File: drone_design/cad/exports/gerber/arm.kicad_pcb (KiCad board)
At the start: 2 copper layers, 245 x 25 mm, 4 parts

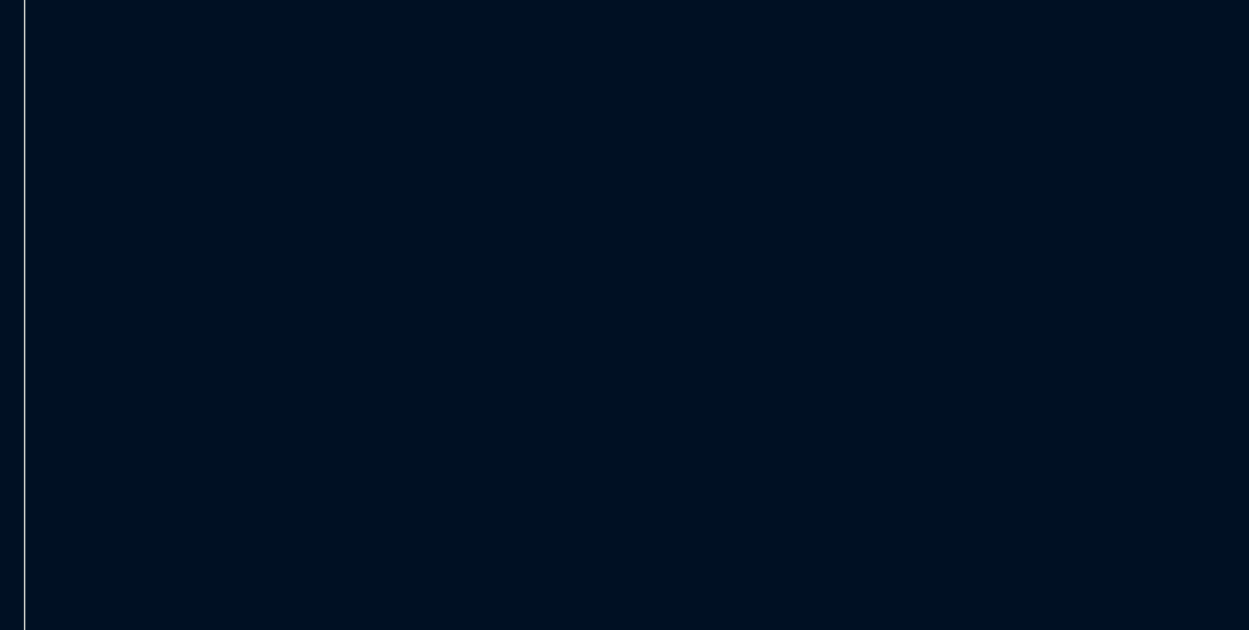
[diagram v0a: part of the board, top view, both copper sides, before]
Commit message: feat: fix ToF bracket alignment, add motor mount to arm tips
- Fix all 6 ToF sensor/bracket positions with correct rotations
  so sensors sit flush against bracket tab faces, sensing outward
- Add circular motor mounting plate at arm tips (25mm dia)
  with 4x M2 bolt holes on 16mm circle + center shaft clearance
- Add matching M2 threaded holes to motor base plate model
- Rebuild all STLs and viewer (68 parts, 15.8 MB total)
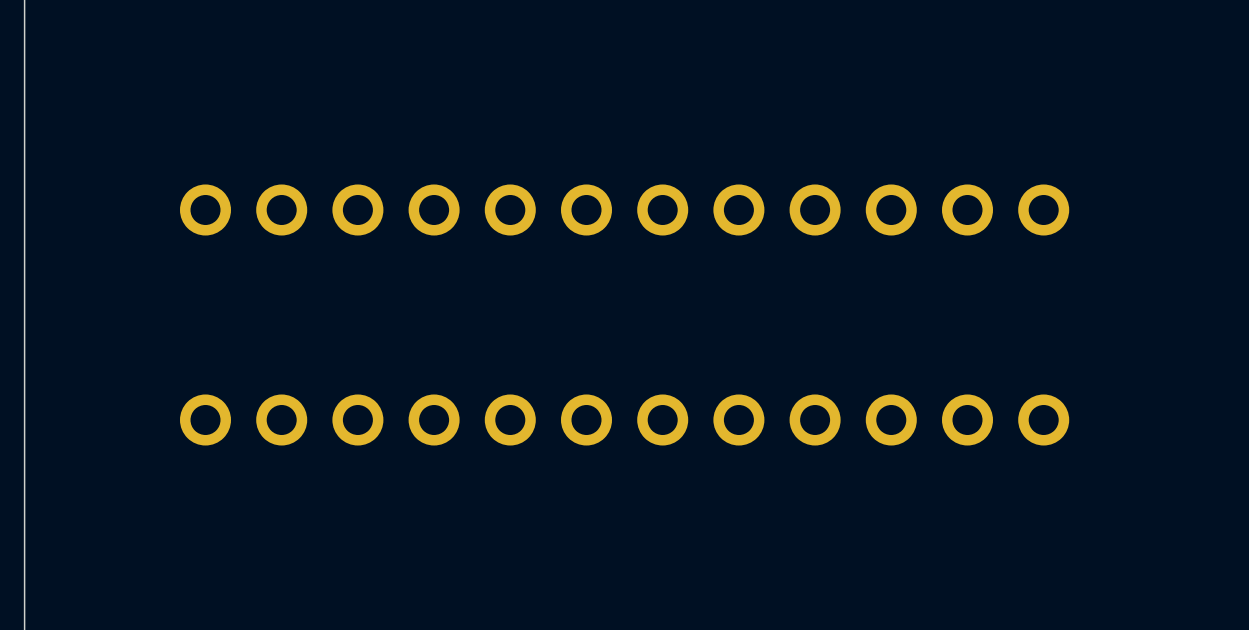
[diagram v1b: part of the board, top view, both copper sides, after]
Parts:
- added ?: , MountingHole:MountingHole_1.0mm, F.Cu at (-103.8, -3.50)
- added ?: , MountingHole:MountingHole_1.0mm, F.Cu at (-101.2, -3.50)
- added ?: , MountingHole:MountingHole_1.0mm, F.Cu at (-98.7, -3.50)
- added ?: , MountingHole:MountingHole_1.0mm, F.Cu at (-96.2, -3.50)
- added ?: , MountingHole:MountingHole_1.0mm, F.Cu at (-93.6, -3.50)
- added ?: , MountingHole:MountingHole_1.0mm, F.Cu at (-91.1, -3.50)
- added ?: , MountingHole:MountingHole_1.0mm, F.Cu at (-88.5, -3.50)
- added ?: , MountingHole:MountingHole_1.0mm, F.Cu at (-116.5, 3.50)
- added ?: , MountingHole:MountingHole_1.0mm, F.Cu at (-113.9, 3.50)
- added ?: , MountingHole:MountingHole_1.0mm, F.Cu at (-111.4, 3.50)
- added ?: , MountingHole:MountingHole_1.0mm, F.Cu at (-108.8, 3.50)
- added ?: , MountingHole:MountingHole_1.0mm, F.Cu at (-106.3, 3.50)
- added ?: , MountingHole:MountingHole_1.0mm, F.Cu at (-103.8, 3.50)
- added ?: , MountingHole:MountingHole_1.0mm, F.Cu at (-101.2, 3.50)
- added ?: , MountingHole:MountingHole_1.0mm, F.Cu at (-98.7, 3.50)
- added ?: , MountingHole:MountingHole_1.0mm, F.Cu at (-96.2, 3.50)
- added ?: , MountingHole:MountingHole_1.0mm, F.Cu at (-93.6, 3.50)
- added ?: , MountingHole:MountingHole_1.0mm, F.Cu at (-91.1, 3.50)
- added ?: , MountingHole:MountingHole_1.0mm, F.Cu at (-88.5, 3.50)
- added ?: , MountingHole:MountingHole_1.0mm, F.Cu at (-116.5, -3.50)
- added ?: , MountingHole:MountingHole_1.0mm, F.Cu at (-113.9, -3.50)
- added ?: , MountingHole:MountingHole_1.0mm, F.Cu at (-111.4, -3.50)
- added ?: , MountingHole:MountingHole_1.0mm, F.Cu at (-108.8, -3.50)
- added ?: , MountingHole:MountingHole_1.0mm, F.Cu at (-106.3, -3.50)
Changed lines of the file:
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@@
+    )
+  )
+  (footprint "MountingHole:MountingHole_1.0mm" (layer "F.Cu")
+    (at -116.4700 -3.5000)
+    (pad "" thru_hole circle (at 0 0) (size 1.70 1.70) (drill 1.00)
+      (layers "*.Cu" "*.Mask")
+    )
+  )
+  (footprint "MountingHole:MountingHole_1.0mm" (layer "F.Cu")
+    (at -113.9300 -3.5000)
+    (pad "" thru_hole circle (at 0 0) (size 1.70 1.70) (drill 1.00)
+      (layers "*.Cu" "*.Mask")
+    )
+  )
+  (footprint "MountingHole:MountingHole_1.0mm" (layer "F.Cu")
+    (at -111.3900 -3.5000)
+    (pad "" thru_hole circle (at 0 0) (size 1.70 1.70) (drill 1.00)
+      (layers "*.Cu" "*.Mask")
+    )
+  )
+  (footprint "MountingHole:MountingHole_1.0mm" (layer "F.Cu")
+    (at -108.8500 -3.5000)
+    (pad "" thru_hole circle (at 0 0) (size 1.70 1.70) (drill 1.00)
+      (layers "*.Cu" "*.Mask")
+    )
+  )
+  (footprint "MountingHole:MountingHole_1.0mm" (layer "F.Cu")
+    (at -106.3100 -3.5000)
+    (pad "" thru_hole circle (at 0 0) (size 1.70 1.70) (drill 1.00)
+      (layers "*.Cu" "*.Mask")
+    )
+  )
+  (footprint "MountingHole:MountingHole_1.0mm" (layer "F.Cu")
+    (at -103.7700 -3.5000)
+    (pad "" thru_hole circle (at 0 0) (size 1.70 1.70) (drill 1.00)
+      (layers "*.Cu" "*.Mask")
+    )
+  )
+  (footprint "MountingHole:MountingHole_1.0mm" (layer "F.Cu")
+    (at -101.2300 -3.5000)
+    (pad "" thru_hole circle (at 0 0) (size 1.70 1.70) (drill 1.00)
+      (layers "*.Cu" "*.Mask")
+    )
+  )
+  (footprint "MountingHole:MountingHole_1.0mm" (layer "F.Cu")
+    (at -98.6900 -3.5000)
+    (pad "" thru_hole circle (at 0 0) (size 1.70 1.70) (drill 1.00)
+      (layers "*.Cu" "*.Mask")
+    )
+  )
+  (footprint "MountingHole:MountingHole_1.0mm" (layer "F.Cu")
+    (at -96.1500 -3.5000)
+    (pad "" thru_hole circle (at 0 0) (size 1.70 1.70) (drill 1.00)
+      (layers "*.Cu" "*.Mask")
+    )
+  )
+  (footprint "MountingHole:MountingHole_1.0mm" (layer "F.Cu")
+    (at -93.6100 -3.5000)
+    (pad "" thru_hole circle (at 0 0) (size 1.70 1.70) (drill 1.00)
+      (layers "*.Cu" "*.Mask")
+    )
+  )
+  (footprint "MountingHole:MountingHole_1.0mm" (layer "F.Cu")
+    (at -91.0700 -3.5000)
+    (pad "" thru_hole circle (at 0 0) (size 1.70 1.70) (drill 1.00)
+      (layers "*.Cu" "*.Mask")
+    )
+  )
+  (footprint "MountingHole:MountingHole_1.0mm" (layer "F.Cu")
+    (at -88.5300 -3.5000)
+    (pad "" thru_hole circle (at 0 0) (size 1.70 1.70) (drill 1.00)
+      (layers "*.Cu" "*.Mask")
+    )
+  )
+  (footprint "MountingHole:MountingHole_1.0mm" (layer "F.Cu")
+    (at -116.4700 3.5000)
+    (pad "" thru_hole circle (at 0 0) (size 1.70 1.70) (drill 1.00)
+      (layers "*.Cu" "*.Mask")
+    )
+  )
+  (footprint "MountingHole:MountingHole_1.0mm" (layer "F.Cu")
+    (at -113.9300 3.5000)
+    (pad "" thru_hole circle (at 0 0) (size 1.70 1.70) (drill 1.00)
+      (layers "*.Cu" "*.Mask")
+    )
+  )
+  (footprint "MountingHole:MountingHole_1.0mm" (layer "F.Cu")
+    (at -111.3900 3.5000)
+    (pad "" thru_hole circle (at 0 0) (size 1.70 1.70) (drill 1.00)
+      (layers "*.Cu" "*.Mask")
+    )
+  )
+  (footprint "MountingHole:MountingHole_1.0mm" (layer "F.Cu")
+    (at -108.8500 3.5000)
+    (pad "" thru_hole circle (at 0 0) (size 1.70 1.70) (drill 1.00)
+      (layers "*.Cu" "*.Mask")
+    )
+  )
+  (footprint "MountingHole:MountingHole_1.0mm" (layer "F.Cu")
+    (at -106.3100 3.5000)
+    (pad "" thru_hole circle (at 0 0) (size 1.70 1.70) (drill 1.00)
+      (layers "*.Cu" "*.Mask")
+    )
+  )
+  (footprint "MountingHole:MountingHole_1.0mm" (layer "F.Cu")
+    (at -103.7700 3.5000)
+    (pad "" thru_hole circle (at 0 0) (size 1.70 1.70) (drill 1.00)
+      (layers "*.Cu" "*.Mask")
+    )
+  )
+  (footprint "MountingHole:MountingHole_1.0mm" (layer "F.Cu")
+    (at -101.2300 3.5000)
+    (pad "" thru_hole circle (at 0 0) (size 1.70 1.70) (drill 1.00)
+      (layers "*.Cu" "*.Mask")
+    )
+  )
+  (footprint "MountingHole:MountingHole_1.0mm" (layer "F.Cu")
+    (at -98.6900 3.5000)
+    (pad "" thru_hole circle (at 0 0) (size 1.70 1.70) (drill 1.00)
+      (layers "*.Cu" "*.Mask")
+    )
+  )
+  (footprint "MountingHole:MountingHole_1.0mm" (layer "F.Cu")
+    (at -96.1500 3.5000)
+    (pad "" thru_hole circle (at 0 0) (size 1.70 1.70) (drill 1.00)
+      (layers "*.Cu" "*.Mask")
+    )
+  )
+  (footprint "MountingHole:MountingHole_1.0mm" (layer "F.Cu")
+    (at -93.6100 3.5000)
+    (pad "" thru_hole circle (at 0 0) (size 1.70 1.70) (drill 1.00)
+      (layers "*.Cu" "*.Mask")
+    )
+  )
+  (footprint "MountingHole:MountingHole_1.0mm" (layer "F.Cu")
+    (at -91.0700 3.5000)
+    (pad "" thru_hole circle (at 0 0) (size 1.70 1.70) (drill 1.00)
+      (layers "*.Cu" "*.Mask")
+    )
+  )
+  (footprint "MountingHole:MountingHole_1.0mm" (layer "F.Cu")
+    (at -88.5300 3.5000)
+    (pad "" thru_hole circle (at 0 0) (size 1.70 1.70) (drill 1.00)
+      (layers "*.Cu" "*.Mask")
     )
   )
